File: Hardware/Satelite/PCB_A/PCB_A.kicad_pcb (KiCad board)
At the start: 2 copper layers, 47 x 47 mm, 40 parts, among them J1 Batería LiPo (Soldada), J2 CONUFL001-SMD, J3 Servo Globo, J4 Conector_PCB_A-B, J5 Servo Paracaídas, Q1 SSM3J338R,LF, SW1 JS102011SAQN, U1 A2235-H, U2 CC1101RGP, U3 0915BM15A0001E, Y1 26 MHz

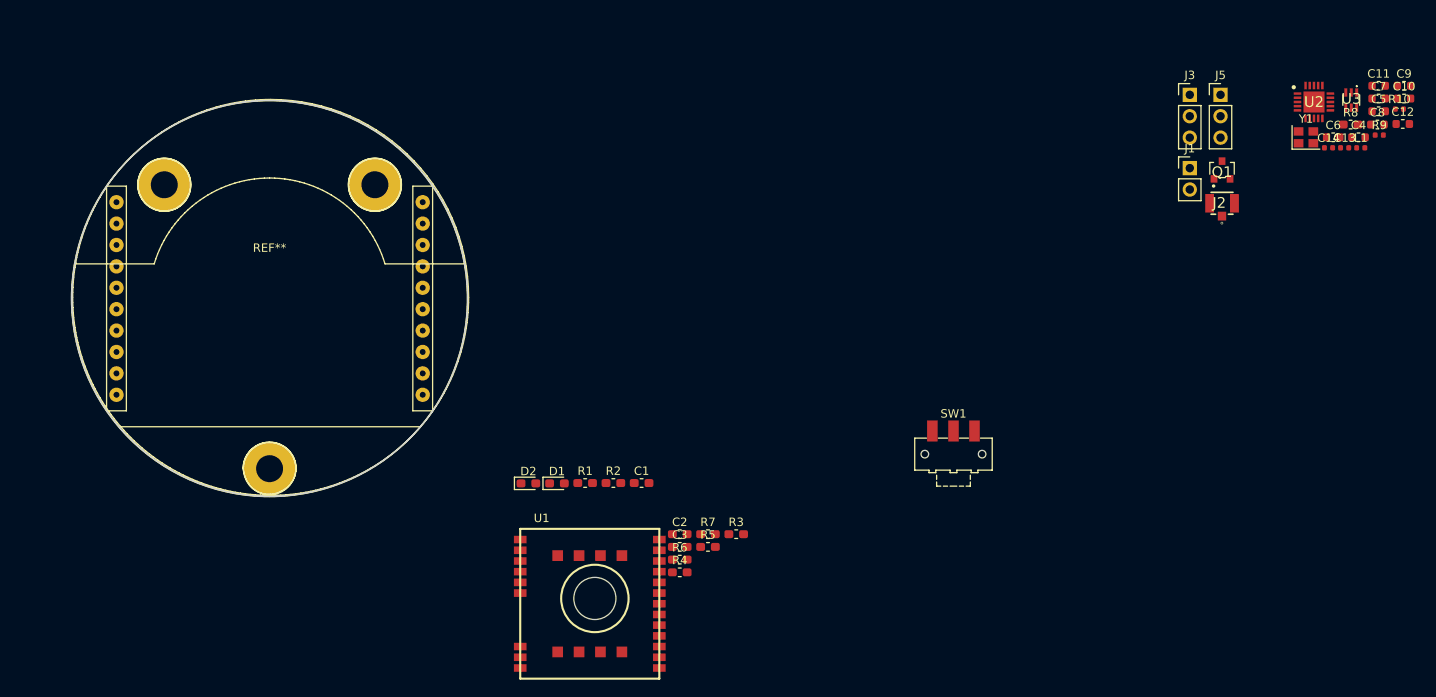
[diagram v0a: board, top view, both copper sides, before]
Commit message: PCB_A modificado coenctor PCB A-B
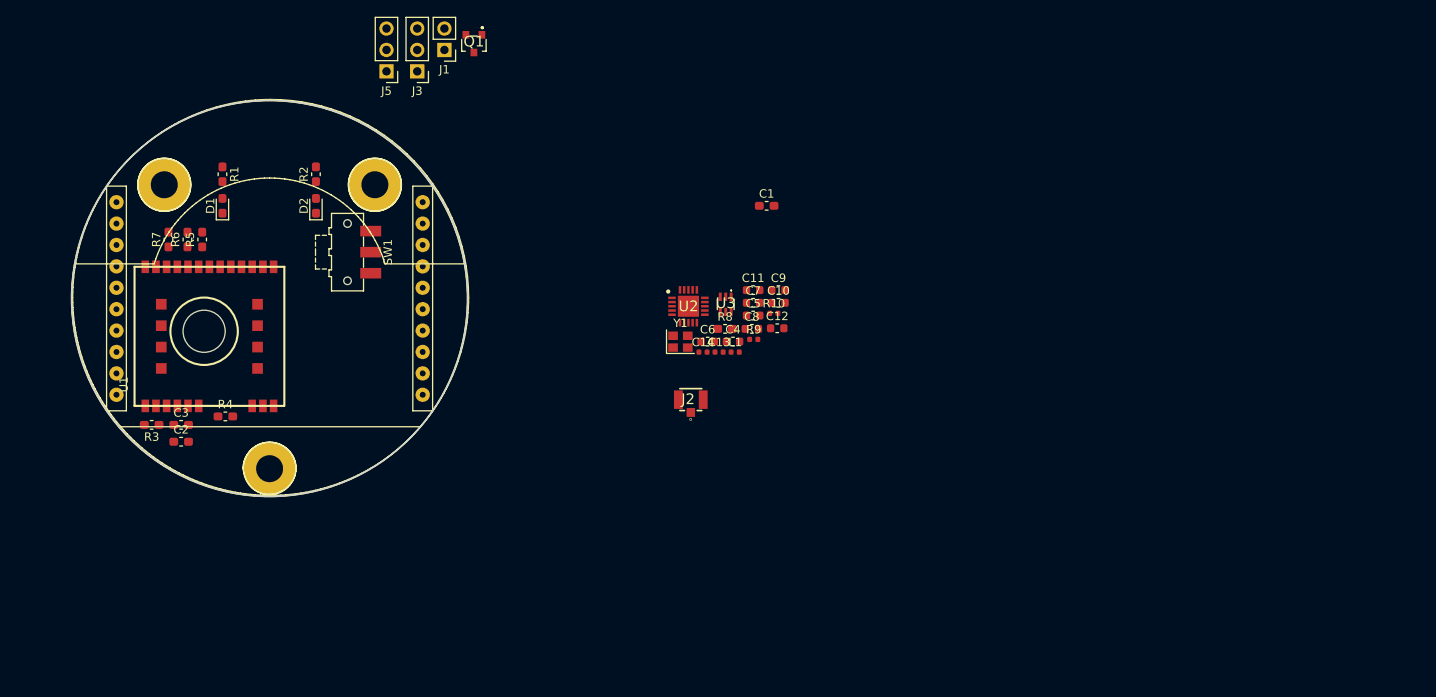
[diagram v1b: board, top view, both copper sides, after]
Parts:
- moved J5 99.0 mm to (13.9, -27.0), turned to 180 degrees
- moved J3 91.7 mm to (17.5, -27.0), turned to 180 degrees
- moved Q1 90.1 mm to (24.2, -30.2), turned to 180 degrees
- moved J1 89.6 mm to (20.8, -29.5), turned to 180 degrees
- moved L1 78.1 mm to (55.3, 6.37)
- moved U3 78.1 mm to (54.1, 0.70)
- moved C10 78.1 mm to (60.4, 0.52)
- moved C11 78.1 mm to (57.4, -0.99)
- moved C12 78.1 mm to (60.3, 3.54)
- moved C13 78.1 mm to (53.4, 6.37)
- moved C14 78.1 mm to (51.4, 6.37)
- moved C4 78.1 mm to (55.0, 5.12)
- moved C5 78.1 mm to (57.4, 2.03)
- moved C6 78.1 mm to (52.0, 5.12)
- moved C7 78.1 mm to (57.4, 0.52)
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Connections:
- J4 pad 11: /GPS_TX -> /P1
- J4 pad 12: /P1 -> /GPS_TX
- J4 pad 13: +3V3_Internal -> Net-(J4-Pad13)
- J4 pad 16: Net-(J4-Pad16) -> +3V3_Internal

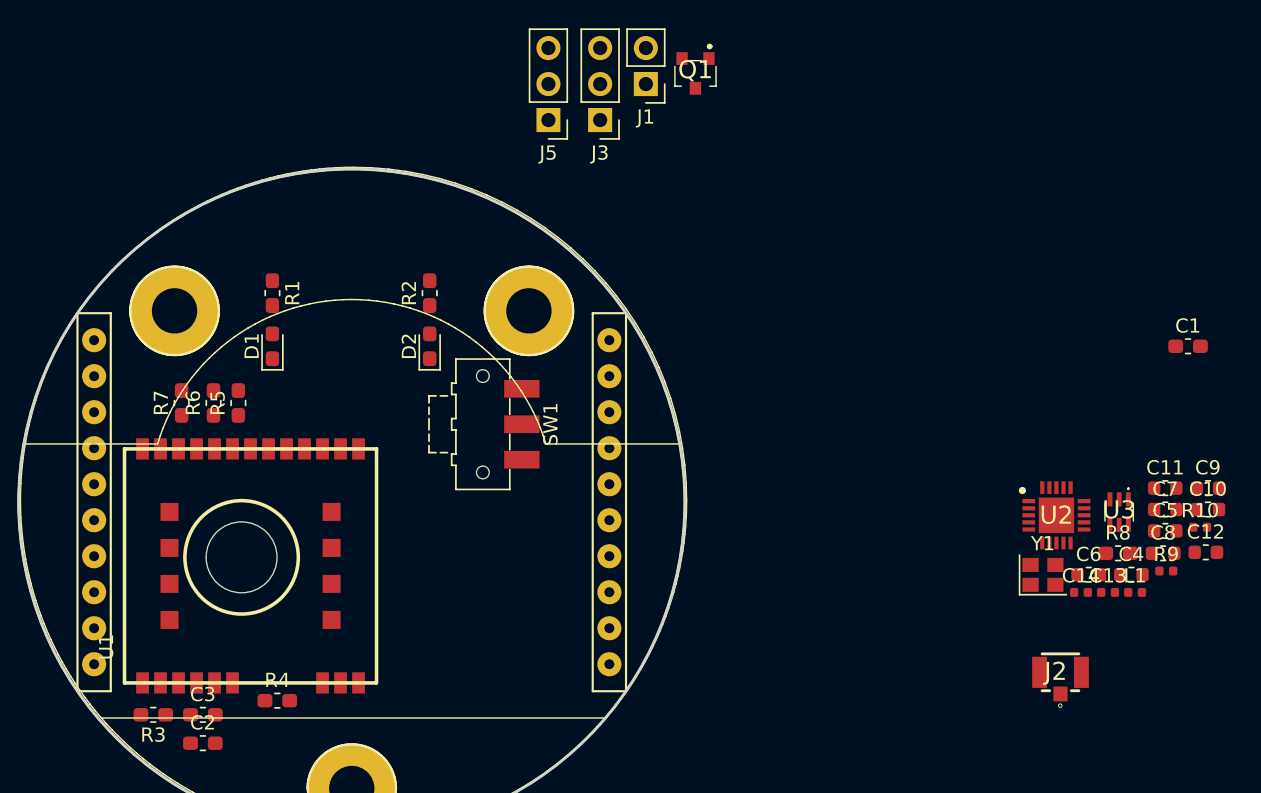
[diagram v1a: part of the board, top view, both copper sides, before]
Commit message: Nueva modificacion en Coenctor PCB A-B
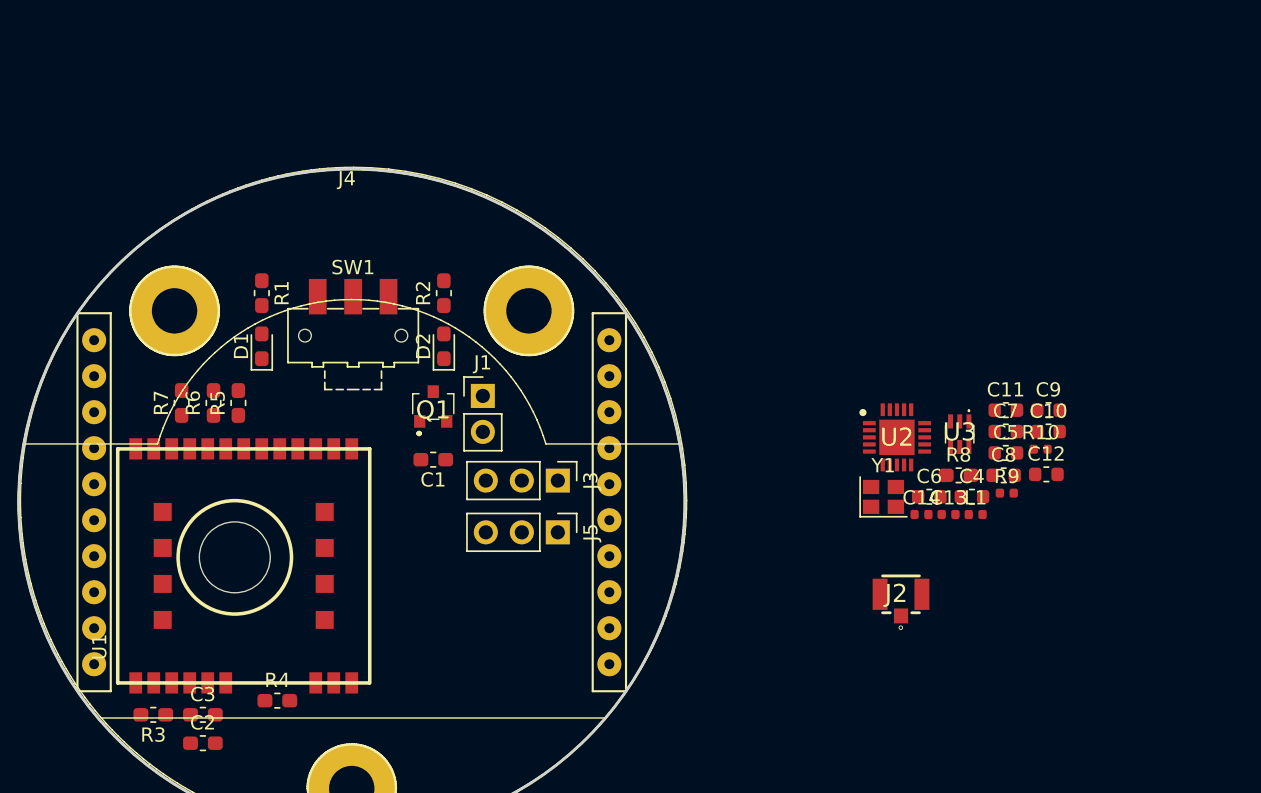
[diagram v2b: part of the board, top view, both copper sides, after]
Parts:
- moved C1 53.8 mm to (5.75, -3.00), turned to 180 degrees
- moved Q1 29.9 mm to (5.75, -6.75), turned to 0 degrees
- moved J5 29.1 mm to (14.5, 2.13), turned to 270 degrees
- moved J3 25.6 mm to (14.5, -1.52), turned to 270 degrees
- moved J1 24.8 mm to (9.25, -7.50), turned to 0 degrees
- moved C10 12.5 mm to (49.2, -4.98)
- moved C11 12.5 mm to (46.1, -6.49)
- moved C12 12.5 mm to (49.0, -1.96)
- moved C13 12.5 mm to (42.1, 0.87)
- moved C14 12.5 mm to (40.2, 0.87)
- moved C4 12.5 mm to (43.8, -0.38)
- moved C5 12.5 mm to (46.1, -3.47)
- moved C6 12.5 mm to (40.7, -0.38)
- moved C7 12.5 mm to (46.1, -4.98)
- moved C8 12.5 mm to (46.0, -1.89)
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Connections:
- J4 pad 10: /S_PARACAIDAS -> /SCLK
- J4 pad 5: /SDO -> /S_GLOBO
- J4 pad 6: /SDI -> /S_PARACAIDAS
- J4 pad 7: /CS -> /SDO
- J4 pad 8: /SCLK -> /SDI
- J4 pad 9: /S_GLOBO -> /CS

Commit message: PCB_A mas cambios
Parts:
- removed SW1: JS102011SAQN, Button_Switch_SMD:SW_SPDT_CK-JS102011SAQN
- added S1: 500SSP1S1M6QEA, SamacSys_Parts:500SSP1S1M6QEA, F.Cu at (0.00, -14.2)
- C10, C11, C12, C4, C5, C6, C7, C8, C9: footprint Capacitor_SMD:C_0603_1608Metric -> Capacitor_SMD:C_0402_1005Metric
- R8: footprint Resistor_SMD:R_0603_1608Metric_Pad1.05x0.95mm_HandSolder -> Resistor_SMD:R_0402_1005Metric
- moved C12 22.5 mm to (29.5, 9.25)
- moved R10 14.7 mm to (39.0, 7.44)
- moved C10 13.2 mm to (39.1, 3.48)
- moved Y1 12.2 mm to (36.5, 11.8)
- moved C9 12.2 mm to (41.0, 2.49)
- moved C11 11.2 mm to (41.0, 3.48)
- moved C6 11.1 mm to (33.2, 7.84)
- moved C13 10.7 mm to (33.2, 6.85)
- moved U2 10.5 mm to (31.9, 3.68)
- moved U3 10.5 mm to (36.4, 3.45)
- moved D2 10.1 mm to (5.25, -21.0), turned to 0 degrees
- moved D1 10.0 mm to (-5.50, -21.0), turned to 180 degrees
- moved J2 10.00 mm to (47.9, 2.40)
- moved R8 9.17 mm to (39.0, 6.45)
- moved C5 8.66 mm to (39.1, 1.50)
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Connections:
- U2 pad 2: /CC1101/SO -> /SDO
- U2 pad 20: /CC1101/SI -> /SDI
- U2 pad 7: GND -> /CS

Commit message: PCB_A terminado
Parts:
- moved J2 42.1 mm to (9.14, 18.9), turned to 180 degrees
- moved C7 38.1 mm to (2.90, 1.47)
- moved C9 37.1 mm to (4.30, 8.24), turned to 270 degrees
- moved C8 36.4 mm to (2.92, 6.46), turned to 180 degrees
- moved Y1 34.5 mm to (2.90, 3.96), turned to 270 degrees
- moved L1 33.7 mm to (9.14, 15.5), turned to 270 degrees
- moved C10 33.7 mm to (5.74, 8.24), turned to 270 degrees
- moved R9 32.8 mm to (9.14, 13.4), turned to 270 degrees
- moved C5 32.8 mm to (6.30, 1.16), turned to 90 degrees
- moved C4 31.0 mm to (8.25, 1.21), turned to 90 degrees
- moved C11 30.6 mm to (11.0, 9.84)
- moved R10 29.5 mm to (10.3, 14.4), turned to 270 degrees
- moved U3 29.1 mm to (8.25, 10.9), turned to 270 degrees
- moved C14 28.6 mm to (12.0, 14.9)
- moved R8 26.9 mm to (12.2, 6.69), turned to 90 degrees
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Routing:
- net GND: track 0.00 -> 145.3 mm, vias 0 -> 18
- net +3V3_Internal: track 0.00 -> 100.7 mm, vias 0 -> 8
- net /GPS/GPS_1V8: track 0.00 -> 45.0 mm, vias 0 -> 2
- net Net-(U1-Pad19): track 0.00 -> 35.9 mm
- net Net-(J4-Pad1): track 0.00 -> 31.1 mm
- net /CS: track 0.00 -> 30.4 mm
- net /SCLK: track 0.00 -> 15.1 mm
- net /P1: track 0.00 -> 12.5 mm
- net Net-(C7-Pad1): track 0.00 -> 11.1 mm
- net /SDO: track 0.00 -> 10.8 mm
- net /SDI: track 0.00 -> 10.4 mm, vias 0 -> 2
- net /GPS_TX: track 0.00 -> 7.60 mm
- net +BATT: track 0.00 -> 6.85 mm
- net Net-(C8-Pad1): track 0.00 -> 5.10 mm
- net /S_GLOBO: track 0.00 -> 3.52 mm
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- added copper zone on B.Cu, net GND
- added copper zone on F.Cu, net GND
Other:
- net class ANT added: clearance 0.2, trace_width 0.4, via_dia 0.8, via_drill 0.4
- net class Alimentacion added: clearance 0.2, trace_width 0.3, via_dia 0.8, via_drill 0.4
- net class Default: trace_width 0.25 -> 0.3
- net class RF_DIF added: clearance 0.2, trace_width 0.25, via_dia 0.8, via_drill 0.4
